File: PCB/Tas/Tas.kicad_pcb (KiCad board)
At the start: 2 copper layers, 14 x 28 mm, 26 parts, among them J1 Shelly 1, J2 Other, J3 USB-C, Q1 PMF170XP,115, Q2 PMF250XNEX, U1 FT231XQ, U2 LMR16006XDDCR

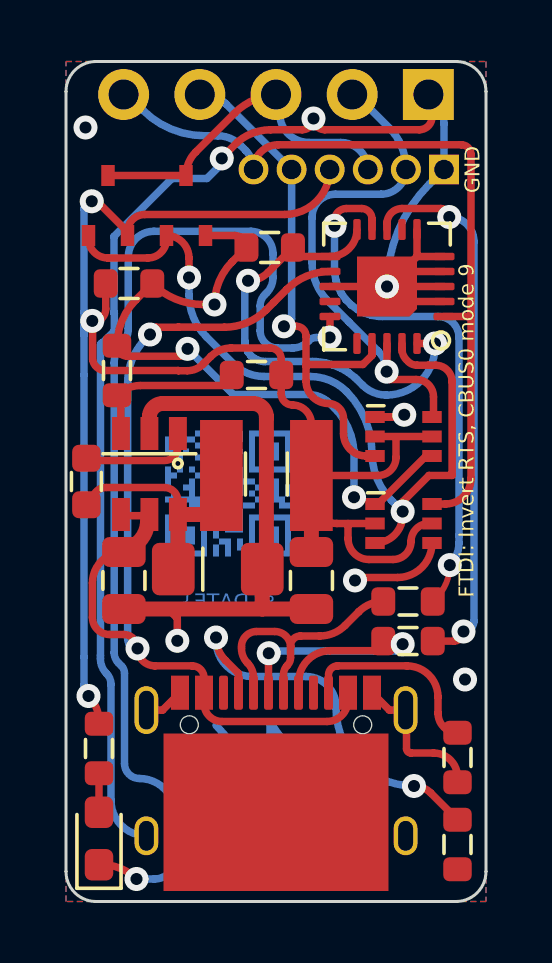
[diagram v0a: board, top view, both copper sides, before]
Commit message: Revised PCB with 7 pin small connector
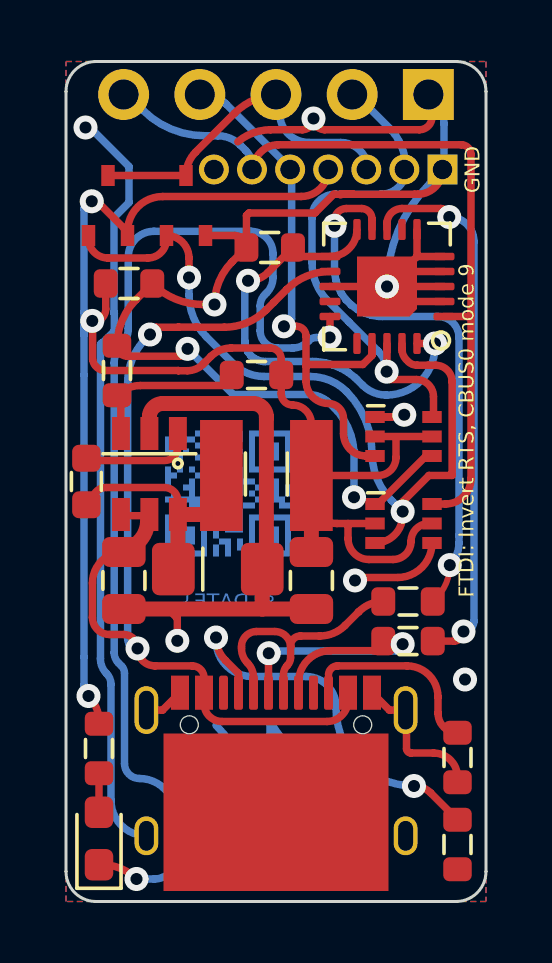
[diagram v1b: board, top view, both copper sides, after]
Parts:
- J2: value Other -> Conn_01x07; footprint RevK:PinHeader_1x06_P1.27mm_Vertical -> RevK:PinHeader_1x07_P1.27mm_Vertical
- moved J2 3.12 mm to (182.6, 58.6), turned to 90 degrees
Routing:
- net GND: track 88.8 -> 96.6 mm, vias 11 -> 10
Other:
- board text added: "${DATE}"

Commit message: Library update
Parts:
- U2: value LMR16006XDDCR -> LMR16006YDDCR
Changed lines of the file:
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@@
     )
   )
-  (property "DATE" "2023-01-27")
+  (property "DATE" "2023-02-07")
   (net 0 "")
   (net 1 "GND")
@@
     (at 172.78 68.75)
     (descr "LMR16006 based fixed regulator")
-    (property "JLCPCB Rotation Offset" "90")
-    (property "LCSC Part #" "C87080")
+    (property "JLCPCB Rotation Offset" "0")
+    (property "LCSC Part #" "C290195")
     (property "Manufacturer" "TI")
-    (property "Part No" "LMR16006XDDCR")
+    (property "Part No" "LMR16006YDDCR")
     (property "Sheetfile" "Tas.kicad_sch")
     (property "Sheetname" "")
@@
       (effects (font (size 0.5 0.5) (thickness 0.08)))
     )
-    (fp_text value "LMR16006XDDCR" (at -2.55 2.65 90) (layer "F.Fab")
+    (fp_text value "LMR16006YDDCR" (at -2.55 2.65 90) (layer "F.Fab")
       (effects (font (size 0.5 0.5) (thickness 0.1)) (justify right))
     )

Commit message: Tweak
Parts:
- moved J2 3.81 mm to (178.7, 58.6)
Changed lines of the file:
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@@
       (layer "F.SilkS" (type "Top Silk Screen"))
       (layer "F.Paste" (type "Top Solder Paste"))
-      (layer "F.Mask" (type "Top Solder Mask") (thickness 0.01))
+      (layer "F.Mask" (type "Top Solder Mask") (color "Purple") (thickness 0.01))
       (layer "F.Cu" (type "copper") (thickness 0.035))
       (layer "dielectric 1" (type "core") (thickness 0.71) (material "FR4") (epsilon_r 4.5) (loss_tangent 0.02))
       (layer "B.Cu" (type "copper") (thickness 0.035))
-      (layer "B.Mask" (type "Bottom Solder Mask") (thickness 0.01))
+      (layer "B.Mask" (type "Bottom Solder Mask") (color "Purple") (thickness 0.01))
       (layer "B.Paste" (type "Bottom Solder Paste"))
       (layer "B.SilkS" (type "Bottom Silk Screen"))
@@
     )
   )
-  (property "DATE" "2023-02-07")
+  (property "DATE" "2023-03-17")
   (net 0 "")
   (net 1 "GND")
@@
     (descr "USB Type C CMT R/A PCB  Mount Socket 16pin Power+Data")
     (tags "USB-C")
+    (property "JLCPCB Rotation Offset" "0")
     (property "LCSC Part #" "C709357")
     (property "Manufacturer" "Valcon")
@@
     (at 172.78 68.75)
     (descr "LMR16006 based fixed regulator")
-    (property "JLCPCB Rotation Offset" "0")
+    (property "JLCPCB Rotation Offset" "180")
     (property "LCSC Part #" "C290195")
     (property "Manufacturer" "TI")
@@
   )
   (footprint "RevK:PinHeader_1x07_P1.27mm_Vertical" (layer "B.Cu")
-    (at 182.55 58.6 90)
+    (at 178.74 58.6 90)
     (descr "Through hole straight pin header, 1x07, 1.27mm pitch, single row")
     (tags "Through hole pin header THT 1x07 1.27mm single row")
+    (property "JLCPCB Rotation Offset" "90")
     (property "LCSC Part #" "C2832274")
     (property "Sheetfile" "Tas.kicad_sch")
@@
       (effects (font (size 1 1) (thickness 0.15)) (justify mirror))
     )
-    (fp_line (start 1.05 0.625) (end 1.05 -8.25) (layer "B.CrtYd") (width 0.12))
-    (fp_line (start 1.05 -8.25) (end -1.05 -8.25) (layer "B.CrtYd") (width 0.12))
-    (fp_line (start 1.05 0.625) (end -1.05 0.625) (layer "B.CrtYd") (width 0.12))
-    (fp_line (start -1.05 -8.25) (end -1.05 0.625) (layer "B.CrtYd") (width 0.12))
-    (fp_line (start -1.05 0.11) (end -0.525 0.635) (layer "B.Fab") (width 0.1))
-    (fp_line (start 1.05 -8.255) (end -1.05 -8.255) (layer "B.Fab") (width 0.1))
-    (fp_line (start -1.05 -8.255) (end -1.05 0.11) (layer "B.Fab") (width 0.1))
-    (fp_line (start -0.525 0.635) (end 1.05 0.635) (layer "B.Fab") (width 0.1))
-    (fp_line (start 1.05 0.635) (end 1.05 -8.255) (layer "B.Fab") (width 0.1))
-    (pad "1" thru_hole rect (at 0 0 90) (size 1 1) (drill 0.65) (layers *.Cu *.Mask)
+    (fp_line (start 1.05 4.435) (end -1.05 4.435) (layer "B.CrtYd") (width 0.12))
+    (fp_line (start 1.05 4.435) (end 1.05 -4.44) (layer "B.CrtYd") (width 0.12))
+    (fp_line (start -1.05 -4.44) (end -1.05 4.435) (layer "B.CrtYd") (width 0.12))
+    (fp_line (start 1.05 -4.44) (end -1.05 -4.44) (layer "B.CrtYd") (width 0.12))
+    (fp_line (start 1.05 -4.445) (end -1.05 -4.445) (layer "B.Fab") (width 0.1))
+    (fp_line (start -0.525 4.445) (end 1.05 4.445) (layer "B.Fab") (width 0.1))
+    (fp_line (start 1.05 4.445) (end 1.05 -4.445) (layer "B.Fab") (width 0.1))
+    (fp_line (start -1.05 -4.445) (end -1.05 3.92) (layer "B.Fab") (width 0.1))
+    (fp_line (start -1.05 3.92) (end -0.525 4.445) (layer "B.Fab") (width 0.1))
+    (pad "1" thru_hole rect (at 0 3.81 90) (size 1 1) (drill 0.65) (layers *.Cu *.Mask)
       (net 1 "GND") (pinfunction "Pin_1") (pintype "passive"))
-    (pad "2" thru_hole oval (at 0 -1.27 90) (size 1 1) (drill 0.65) (layers *.Cu *.Mask)
+    (pad "2" thru_hole oval (at 0 2.54 90) (size 1 1) (drill 0.65) (layers *.Cu *.Mask)
       (net 5 "GPIO0") (pinfunction "Pin_2") (pintype "passive"))
-    (pad "3" thru_hole oval (at 0 -2.54 90) (size 1 1) (drill 0.65) (layers *.Cu *.Mask)
+    (pad "3" thru_hole oval (at 0 1.27 90) (size 1 1) (drill 0.65) (layers *.Cu *.Mask)
       (net 14 "Net-(J1-Pad3)") (pinfunction "Pin_3") (pintype "passive"))
-    (pad "4" thru_hole oval (at 0 -3.81 90) (size 1 1) (drill 0.65) (layers *.Cu *.Mask)
+    (pad "4" thru_hole oval (at 0 0 90) (size 1 1) (drill 0.65) (layers *.Cu *.Mask)
       (net 4 "+3V3") (pinfunction "Pin_4") (pintype "passive"))
-    (pad "5" thru_hole oval (at 0 -5.08 90) (size 1 1) (drill 0.65) (layers *.Cu *.Mask)
+    (pad "5" thru_hole oval (at 0 -1.27 90) (size 1 1) (drill 0.65) (layers *.Cu *.Mask)
       (net 3 "RXD") (pinfunction "Pin_5") (pintype "passive"))
-    (pad "6" thru_hole oval (at 0 -6.35 90) (size 1 1) (drill 0.65) (layers *.Cu *.Mask)
+    (pad "6" thru_hole oval (at 0 -2.54 90) (size 1 1) (drill 0.65) (layers *.Cu *.Mask)
       (net 6 "TXD") (pinfunction "Pin_6") (pintype "passive"))
-    (pad "7" thru_hole oval (at 0 -7.62 90) (size 1 1) (drill 0.65) (layers *.Cu *.Mask)
+    (pad "7" thru_hole oval (at 0 -3.81 90) (size 1 1) (drill 0.65) (layers *.Cu *.Mask)
       (net 26 "unconnected-(J2-Pad7)") (pinfunction "Pin_7") (pintype "passive+no_connect"))
     (model "${KICAD6_3DMODEL_DIR}/Connector_PinHeader_1.27mm.3dshapes/PinHeader_1x07_P1.27mm_Vertical.wrl"
-      (offset (xyz 0 0 0))
-      (scale (xyz 1 1 1))
-      (rotate (xyz 0 0 0))
+      (offset (xyz 0 3.81 0))
+      (scale (xyz 1 1 1))
+      (rotate (xyz 0 0 0))

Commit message: Tidy
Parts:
- Art2: footprint RevK:QR-Tas -> RevK:QR-TAS
- D1, D2: footprint RevK:SOT-363_SC-70-6-Rot -> RevK:SOT-363_SC-70-6
- turned D1 to 0 degrees
- turned D2 to 0 degrees
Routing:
- net GND: vias 10 -> 9
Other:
- board text added: "${CURRENT_DATE}"
- board text added: "⏚"
- board text removed: "${DATE}"
- board text removed: "GND"

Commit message: SIlk
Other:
- board text added: "5060634238014"

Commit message: Replaced old board with new
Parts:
- removed C2: 100nF, RevK:C_0603_
- removed C3: 2.2uF, RevK:C_0805_
- removed C4: 10uF, RevK:C_0805_
- removed D3: LED, LED_SMD:LED_0603_1608Metric_Pad1.05x0.95mm_HandSolder
- removed L1: 6.8uH, RevK:L_4x4_
- removed R5: 680R, RevK:R_0603
- removed U2: LMR16006YDDCR, RevK:SOT-23-Thin-6-Reg
- added C6: 10uF 50V, RevK:C_0603_, F.Cu at (174.2, 71.6)
- added C7: 10uF 6.3V, RevK:C_0603_, F.Cu at (174.2, 66.6)
- added C8: 100nF, RevK:C_0603_, F.Cu at (174.9, 69.1)
- added L2: 10uH, RevK:L_4x4_, F.Cu at (177.5, 69.1)
- added R10: 1M, RevK:R_0402_, F.Cu at (172.1, 71.6)
- added R11: 220R, RevK:R_0402, F.Cu at (177.1, 65.3)
- added R8: 124k, RevK:R_0402_, F.Cu at (171.0, 69.1)
- added R9: 39k2, RevK:R_0402_, F.Cu at (172.1, 66.6)
- added U3: MD8942, RevK:SOT-23-6-MD8942, F.Cu at (172.9, 69.1)
- C1, C5: footprint RevK:C_0603 -> RevK:C_0402
- D4: value Schottky -> RGB; footprint RevK:D_1206_ -> RevK:LED-RGB-1.6x1.6
- J2: moved to F.Cu
- R1, R2, R3, R4: footprint RevK:R_0603 -> RevK:R_0402
- R6: value 100k 1% -> 680R; footprint RevK:R_0603 -> RevK:R_0402
- R7: value 30k 1% -> 2K; footprint RevK:R_0603 -> RevK:R_0402
- moved R1 10.4 mm to (175.7, 73.7), turned to 90 degrees
- moved D4 7.52 mm to (175.3, 64.4), turned to -90 degrees
- moved R2 6.26 mm to (178.7, 73.7), turned to -90 degrees
- moved R7 5.69 mm to (177.1, 63.5), turned to 0 degrees
- moved R3 4.75 mm to (176.7, 73.7), turned to 90 degrees
- moved R4 3.75 mm to (177.7, 73.7), turned to 90 degrees
- moved J2 3.63 mm to (175.1, 58.5)
- moved C5 3.05 mm to (173.3, 65.2), turned to 180 degrees
- moved Q1 1.40 mm to (171.5, 61.2)
- moved Q2 1.40 mm to (174.1, 61.2)
- moved R6 1.29 mm to (177.1, 64.4), turned to 0 degrees
- moved C1 0.73 mm to (177.2, 60.6)
- moved Art2 0.45 mm to (175.0, 69.6), turned to 90 degrees
- moved D1 0.36 mm to (181.6, 70.5)
- moved D2 0.36 mm to (181.6, 67.6)
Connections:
- R6 pad 1: +3V3 -> Net-(D4-RK)
- R6 pad 2: Net-(U2-FB) -> Net-(U1-CBUS0)
- R7 pad 1: GND -> Net-(D4-GK)
- R7 pad 2: Net-(U2-FB) -> Net-(U1-CBUS1)
- U1 pad 14: unconnected-(U1-CBUS1-Pad14) -> Net-(U1-CBUS1)
- U1 pad 15: Net-(D3-K) -> Net-(U1-CBUS0)
- U1 pad 16: unconnected-(U1-CBUS3-Pad16) -> Net-(U1-CBUS3)
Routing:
- net GND: track 96.6 -> 49.9 mm, vias 9 -> 7
- net Net-(D3-K): track 36.1 -> 0.00 mm, vias 2 -> 0
- net +3V3: track 55.1 -> 32.0 mm, vias 3 -> 1
- net RXD: track 18.6 -> 35.1 mm
- net Net-(J3-CC1): track 13.3 -> 1.79 mm, vias 2 -> 0
- net GPIO0: track 16.9 -> 26.6 mm
- net D+: track 18.3 -> 25.1 mm
- net Net-(J3-D+-PadA6): track 10.8 -> 4.34 mm, vias 2 -> 0
- net Net-(U1-3V3OUT): track 15.3 -> 9.03 mm
- net Net-(U2-FB): track 5.21 -> 0.00 mm
- net TXD: track 26.6 -> 31.3 mm
- net Net-(J3-D--PadA7): track 9.14 -> 4.50 mm
- net VBUS: track 33.0 -> 28.6 mm, vias 2 -> 3
- net Net-(J3-CC2): track 5.90 -> 1.79 mm
- net D-: track 18.1 -> 21.7 mm
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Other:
- board text added: "FTDI: Invert RTS"
- board text added: "Tasmotiser"
- board text removed: "FTDI: Invert RTS, CBUS0 mode 9"

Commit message: New reg
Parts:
- removed Art2: QR, RevK:QR-TAS
- moved Art1 10.5 mm to (174.5, 68.9), turned to 90 degrees
- moved R4 9.66 mm to (171.2, 80.8)
- moved R3 6.22 mm to (171.2, 76.6)
- moved R9 1.30 mm to (171.0, 67.3), turned to 90 degrees
- moved R10 1.30 mm to (171.0, 70.9), turned to 90 degrees
- moved R1 0.97 mm to (176.2, 74.5), turned to 0 degrees
- moved R2 0.94 mm to (178.2, 74.5), turned to 0 degrees
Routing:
- net D+: track 25.1 -> 36.8 mm
- net Net-(J3-D+-PadA6): track 4.34 -> 14.4 mm, vias 0 -> 2
- net D-: track 21.7 -> 29.3 mm
- net Net-(J3-D--PadA7): track 4.50 -> 10.7 mm, vias 0 -> 2
- net GND: track 49.9 -> 44.7 mm, vias 7 -> 8
- net RXD: track 35.1 -> 35.7 mm
